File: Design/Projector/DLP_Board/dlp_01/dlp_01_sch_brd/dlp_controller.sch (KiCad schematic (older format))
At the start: 0 parts

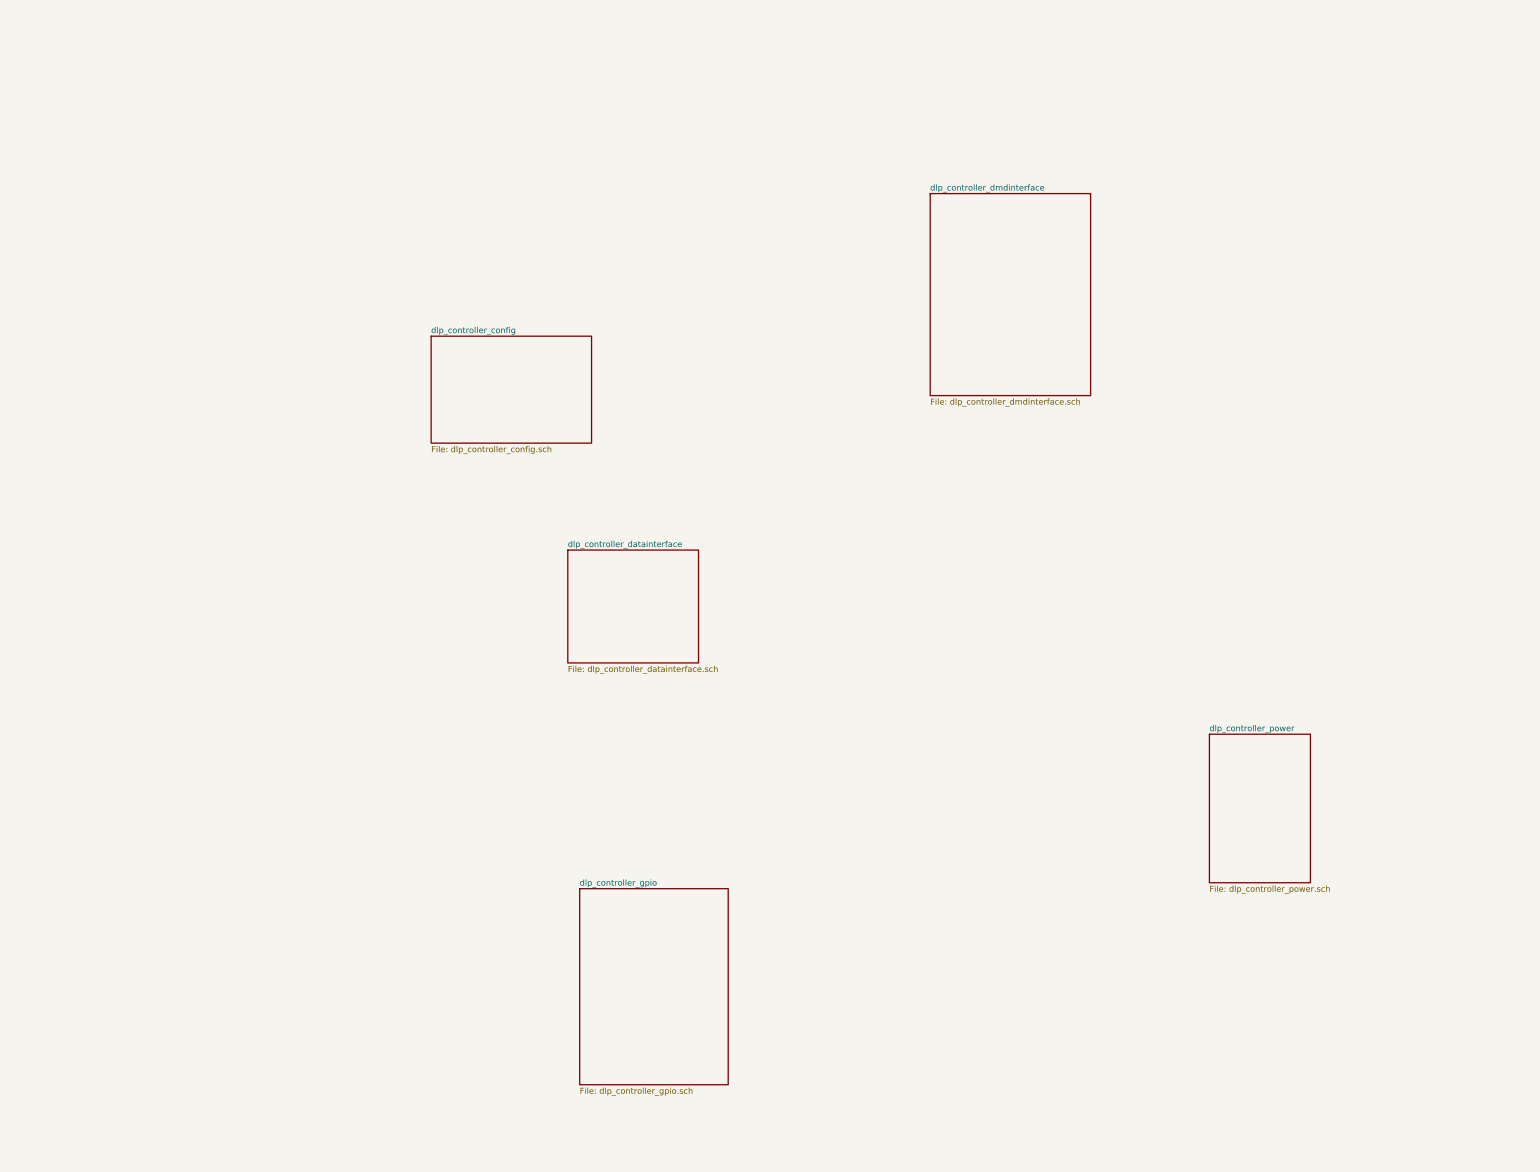
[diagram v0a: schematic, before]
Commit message: Updated schematic with changes pulling together top level design
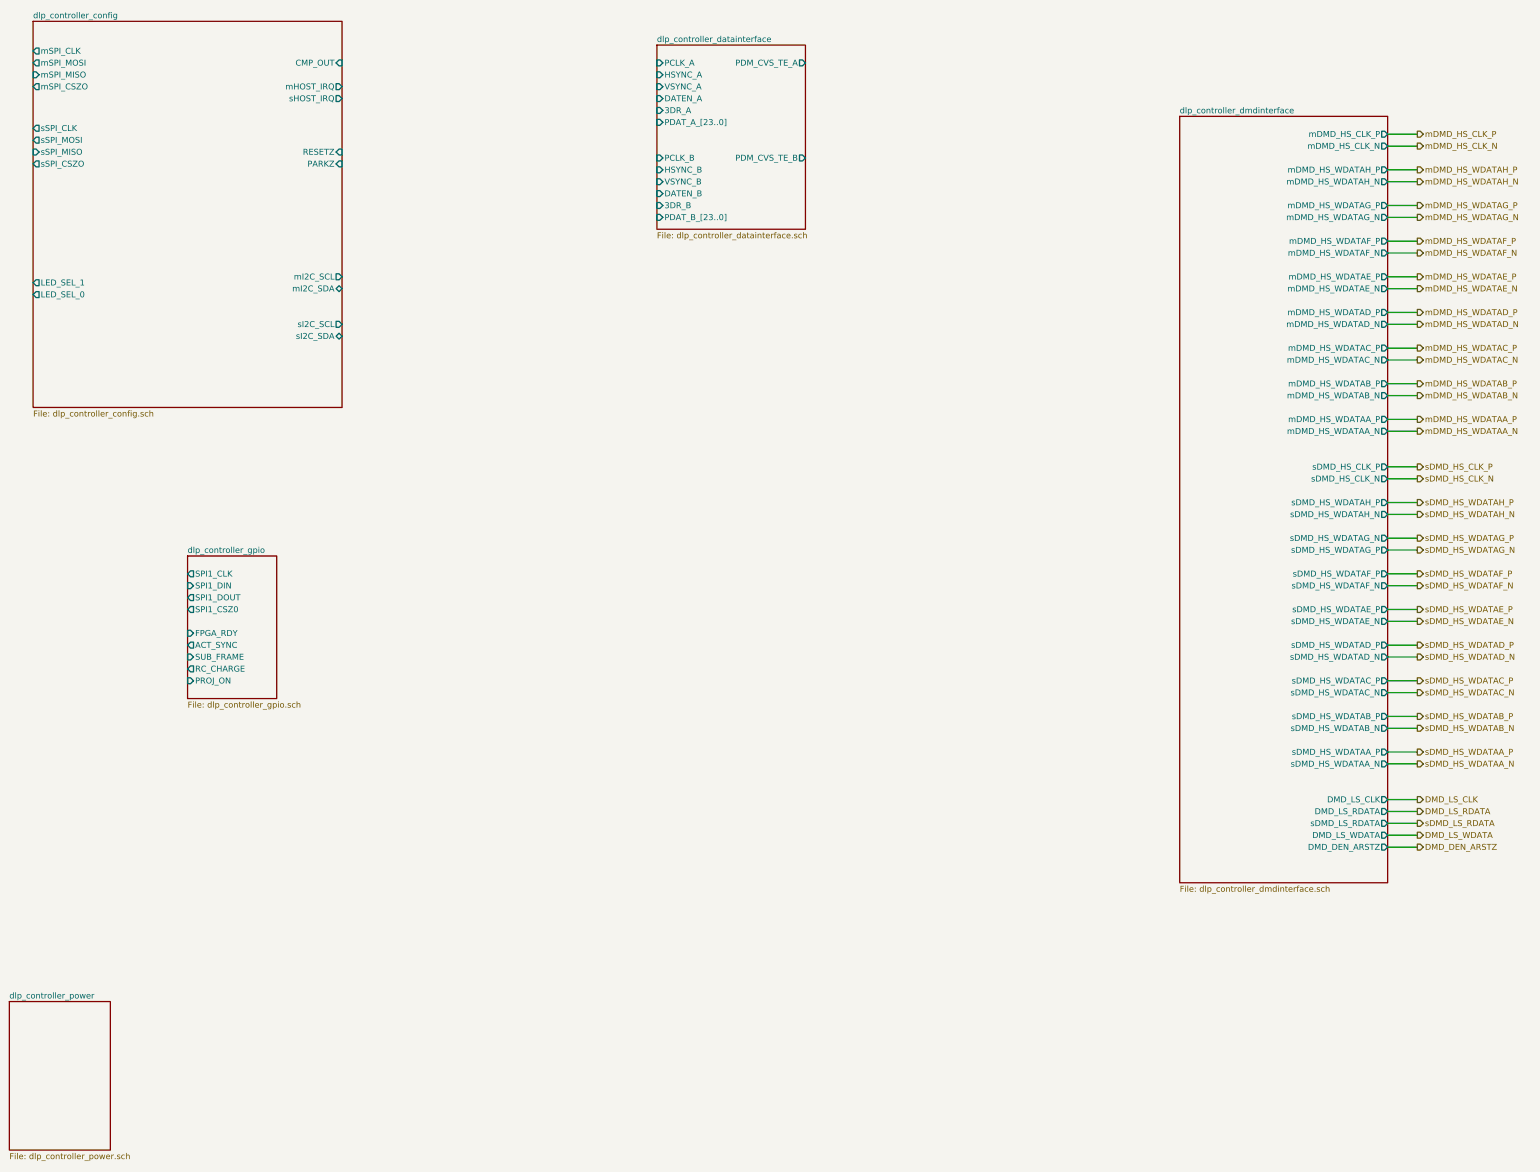
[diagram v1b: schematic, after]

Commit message: Ongoing updates the schematics
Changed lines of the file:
@@
 $EndSheet
 $Sheet
-S 1600 1050 2600 3250
+S 2350 1350 1500 2350
 U 5E32D14B
 F0 "dlp_controller_config" 50
 F1 "dlp_controller_config.sch" 50
-F2 "CMP_OUT" I R 4200 1400 50
-F3 "LED_SEL_0" O L 1600 3350 50
-F4 "LED_SEL_1" O L 1600 3250 50
-F5 "mSPI_CLK" O L 1600 1300 50
-F6 "mSPI_MOSI" O L 1600 1400 50
-F7 "mSPI_CSZO" O L 1600 1600 50
-F8 "mSPI_MISO" I L 1600 1500 50
-F9 "mI2C_SCL" O R 4200 3200 50
-F10 "mI2C_SDA" B R 4200 3300 50
-F11 "sSPI_CLK" O L 1600 1950 50
-F12 "sSPI_MOSI" O L 1600 2050 50
-F13 "sSPI_CSZO" O L 1600 2250 50
-F14 "sSPI_MISO" I L 1600 2150 50
-F15 "sI2C_SCL" O R 4200 3600 50
-F16 "sI2C_SDA" B R 4200 3700 50
-F17 "sHOST_IRQ" O R 4200 1700 50
-F18 "mHOST_IRQ" O R 4200 1600 50
-F19 "PARKZ" I R 4200 2250 50
-F20 "RESETZ" I R 4200 2150 50
+F2 "CMP_OUT" I R 3850 1700 50
+F3 "LED_SEL_0" O L 2350 3350 50
+F4 "LED_SEL_1" O L 2350 3250 50
+F5 "mSPI_CLK" O L 2350 1600 50
+F6 "mSPI_MOSI" O L 2350 1700 50
+F7 "mSPI_CSZO" O L 2350 1900 50
+F8 "mSPI_MISO" I L 2350 1800 50
+F9 "mI2C_SCL" O R 3850 2950 50
+F10 "mI2C_SDA" B R 3850 3050 50
+F11 "sSPI_CLK" O L 2350 2250 50
+F12 "sSPI_MOSI" O L 2350 2350 50
+F13 "sSPI_CSZO" O L 2350 2550 50
+F14 "sSPI_MISO" I L 2350 2450 50
+F15 "sI2C_SCL" O R 3850 3300 50
+F16 "sI2C_SDA" B R 3850 3400 50
+F17 "sHOST_IRQ" O R 3850 2000 50
+F18 "mHOST_IRQ" O R 3850 1900 50
+F19 "PARKZ" I R 3850 2550 50
+F20 "RESETZ" I R 3850 2450 50
 $EndSheet
 $Sheet
-S 6850 1250 1250 1550
+S 7600 1750 1250 1550
 U 5E8F10AD
 F0 "dlp_controller_datainterface" 50
 F1 "dlp_controller_datainterface.sch" 50
-F2 "PCLK_B" I L 6850 2200 50
-F3 "PDM_CVS_TE_B" O R 8100 2200 50
-F4 "VSYNC_B" I L 6850 2400 50
-F5 "HSYNC_B" I L 6850 2300 50
-F6 "DATEN_B" I L 6850 2500 50
-F7 "PDAT_B_[23..0]" I L 6850 2700 50
-F8 "PCLK_A" I L 6850 1400 50
-F9 "PDM_CVS_TE_A" O R 8100 1400 50
-F10 "VSYNC_A" I L 6850 1600 50
-F11 "HSYNC_A" I L 6850 1500 50
-F12 "DATEN_A" I L 6850 1700 50
-F13 "PDAT_A_[23..0]" I L 6850 1900 50
-F14 "3DR_A" I L 6850 1800 50
-F15 "3DR_B" I L 6850 2600 50
+F2 "PCLK_B" I L 7600 2700 50
+F3 "PDM_CVS_TE_B" O R 8850 2700 50
+F4 "VSYNC_B" I L 7600 2900 50
+F5 "HSYNC_B" I L 7600 2800 50
+F6 "DATEN_B" I L 7600 3000 50
+F7 "PDAT_B_[23..0]" I L 7600 3200 50
+F8 "PCLK_A" I L 7600 1900 50
+F9 "PDM_CVS_TE_A" O R 8850 1900 50
+F10 "VSYNC_A" I L 7600 2100 50
+F11 "HSYNC_A" I L 7600 2000 50
+F12 "DATEN_A" I L 7600 2200 50
+F13 "PDAT_A_[23..0]" I L 7600 2400 50
+F14 "3DR_A" I L 7600 2300 50
+F15 "3DR_B" I L 7600 3100 50
 $EndSheet
 Text HLabel 13250 2300 2    50   Output ~ 0
@@
 Wire Wire Line
 	13000 8000 13250 8000
+Text HLabel 2700 6000 0    50   Output ~ 0
+SPI1_CSZ0
+Wire Wire Line
+	2900 6000 2700 6000
+Text HLabel 2700 5900 0    50   Output ~ 0
+SPI1_DOUT
+Text HLabel 2700 5700 0    50   Output ~ 0
+SPI1_CLK
+Text HLabel 2700 5800 0    50   Input ~ 0
+SPI1_DIN
+Wire Wire Line
+	2700 5900 2900 5900
+Wire Wire Line
+	2700 5700 2900 5700
+Wire Wire Line
+	2700 5800 2900 5800
+Text HLabel 2700 6200 0    50   Input ~ 0
+FPGA_RDY
+Text HLabel 2700 6300 0    50   Output ~ 0
+ACT_SYNC
+Text HLabel 2700 6400 0    50   Input ~ 0
+SUB_FRAME
+Text HLabel 2700 6500 0    50   Output ~ 0
+RC_CHARGE
+Text HLabel 2700 6600 0    50   Input ~ 0
+PROJ_ON
+Wire Wire Line
+	2700 6200 2900 6200
+Wire Wire Line
+	2900 6300 2700 6300
+Wire Wire Line
+	2700 6400 2900 6400
+Wire Wire Line
+	2900 6500 2700 6500
+Wire Wire Line
+	2700 6600 2900 6600
+Text HLabel 7300 2700 0    50   Input ~ 0
+PCLK_B
+Text HLabel 9150 2700 2    50   Output ~ 0
+PDM_CVS_TE_B
+Text HLabel 7300 2900 0    50   Input ~ 0
+VSYNC_B
+Text HLabel 7300 2800 0    50   Input ~ 0
+HSYNC_B
+Text HLabel 7300 3000 0    50   Input ~ 0
+DATEN_B
+Text HLabel 7300 3200 0    50   Input ~ 0
+PDAT_B_[23..0]
+Text HLabel 7300 3100 0    50   Input ~ 0
+3DR_B
+Text HLabel 7300 1900 0    50   Input ~ 0
+PCLK_A
+Text HLabel 9150 1900 2    50   Output ~ 0
+PDM_CVS_TE_A
+Text HLabel 7300 2100 0    50   Input ~ 0
+VSYNC_A
+Text HLabel 7300 2000 0    50   Input ~ 0
+HSYNC_A
+Text HLabel 7300 2200 0    50   Input ~ 0
+DATEN_A
+Text HLabel 7300 2400 0    50   Input ~ 0
+PDAT_A_[23..0]
+Text HLabel 7300 2300 0    50   Input ~ 0
+3DR_A
+Wire Wire Line
+	8850 1900 9150 1900
+Wire Wire Line
+	8850 2700 9150 2700
+Wire Wire Line
+	7300 1900 7600 1900
+Wire Wire Line
+	7300 2700 7600 2700
+Wire Wire Line
+	7300 2000 7600 2000
+Wire Wire Line
+	7300 2100 7600 2100
+Wire Wire Line
+	7300 2200 7600 2200
+Wire Wire Line
+	7600 2300 7300 2300
+Wire Wire Line
+	7300 2800 7600 2800
+Wire Wire Line
+	7300 2900 7600 2900
+Wire Wire Line
+	7600 3000 7300 3000
+Wire Wire Line
+	7300 3100 7600 3100
+Wire Bus Line
+	7300 2400 7600 2400
+Wire Bus Line
+	7300 3200 7600 3200
+Text HLabel 2050 1600 0    50   Output ~ 0
+mSPI_CLK
+Text HLabel 2050 1700 0    50   Output ~ 0
+mSPI_MOSI
+Text HLabel 2050 1900 0    50   Output ~ 0
+mSPI_CSZO
+Text HLabel 2050 1800 0    50   Input ~ 0
+mSPI_MISO
+Wire Wire Line
+	2050 1600 2350 1600
+Wire Wire Line
+	2050 1700 2350 1700
+Text HLabel 4150 2950 2    50   Output ~ 0
+mI2C_SCL
+Text HLabel 4150 3050 2    50   BiDi ~ 0
+mI2C_SDA
+Text HLabel 4150 1900 2    50   Output ~ 0
+mHOST_IRQ
+Text HLabel 4150 1700 2    50   Input ~ 0
+CMP_OUT
+Text HLabel 2050 3250 0    50   Output ~ 0
+LED_SEL_0
+Text HLabel 2050 3350 0    50   Output ~ 0
+LED_SEL_1
+Text HLabel 2050 2250 0    50   Output ~ 0
+sSPI_CLK
+Text HLabel 2050 2350 0    50   Output ~ 0
+sSPI_MOSI
+Text HLabel 2050 2550 0    50   Output ~ 0
+sSPI_CSZO
+Text HLabel 2050 2450 0    50   Input ~ 0
+sSPI_MISO
+Text HLabel 4150 2000 2    50   Output ~ 0
+sHOST_IRQ
+Text HLabel 4150 3300 2    50   Output ~ 0
+sI2C_SCL
+Text HLabel 4150 3400 2    50   BiDi ~ 0
+sI2C_SDA
+Text HLabel 4150 2550 2    50   Input ~ 0
+PARKZ
+Text HLabel 4150 2450 2    50   Input ~ 0
+RESETZ
+Wire Wire Line
+	3850 1700 4150 1700
+Wire Wire Line
+	2050 1800 2350 1800
+Wire Wire Line
+	2050 1900 2350 1900
+Wire Wire Line
+	2050 2250 2350 2250
+Wire Wire Line
+	2350 2350 2050 2350
+Wire Wire Line
+	2050 2450 2350 2450
+Wire Wire Line
+	2350 2550 2050 2550
+Wire Wire Line
+	2050 3250 2350 3250
+Wire Wire Line
+	2350 3350 2050 3350
+Wire Wire Line
+	3850 1900 4150 1900
+Wire Wire Line
+	4150 2000 3850 2000
+Wire Wire Line
+	3850 2450 4150 2450
+Wire Wire Line
+	4150 2550 3850 2550
+Wire Wire Line
+	3850 2950 4150 2950
+Wire Wire Line
+	3850 3050 4150 3050
+Wire Wire Line
+	3850 3300 4150 3300
+Wire Wire Line
+	4150 3400 3850 3400
 $EndSCHEMATC

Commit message: More updates in the DLP board
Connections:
- no-connect marks 0 -> 8
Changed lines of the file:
@@
 F0 "dlp_controller_config" 50
 F1 "dlp_controller_config.sch" 50
-F2 "CMP_OUT" I R 3850 1700 50
+F2 "CMP_OUT" I R 3850 1550 50
 F3 "LED_SEL_0" O L 2350 3350 50
 F4 "LED_SEL_1" O L 2350 3250 50
@@
 F7 "mSPI_CSZO" O L 2350 1900 50
 F8 "mSPI_MISO" I L 2350 1800 50
-F9 "mI2C_SCL" O R 3850 2950 50
-F10 "mI2C_SDA" B R 3850 3050 50
-F11 "sSPI_CLK" O L 2350 2250 50
-F12 "sSPI_MOSI" O L 2350 2350 50
-F13 "sSPI_CSZO" O L 2350 2550 50
-F14 "sSPI_MISO" I L 2350 2450 50
-F15 "sI2C_SCL" O R 3850 3300 50
-F16 "sI2C_SDA" B R 3850 3400 50
-F17 "sHOST_IRQ" O R 3850 2000 50
-F18 "mHOST_IRQ" O R 3850 1900 50
-F19 "PARKZ" I R 3850 2550 50
-F20 "RESETZ" I R 3850 2450 50
+F9 "sSPI_CLK" O L 2350 2250 50
+F10 "sSPI_MOSI" O L 2350 2350 50
+F11 "sSPI_CSZO" O L 2350 2550 50
+F12 "sSPI_MISO" I L 2350 2450 50
+F13 "sHOST_IRQ" O R 3850 1850 50
+F14 "mHOST_IRQ" O R 3850 1750 50
+F15 "PARKZ" I R 3850 2200 50
+F16 "RESETZ" I R 3850 2100 50
+F17 "mI2C0_SCL" O R 3850 2450 50
+F18 "mI2C0_SDA" B R 3850 2550 50
+F19 "mI2C1_SCL" O R 3850 2750 50
+F20 "mI2C1_SDA" B R 3850 2850 50
+F21 "sI2C0_SCL" O R 3850 3100 50
+F22 "sI2C0_SDA" B R 3850 3200 50
+F23 "sI2C1_SCL" O R 3850 3400 50
+F24 "sI2C1_SDA" B R 3850 3500 50
 $EndSheet
 $Sheet
@@
 Wire Bus Line
 	7300 3200 7600 3200
-Text HLabel 2050 1600 0    50   Output ~ 0
-mSPI_CLK
-Text HLabel 2050 1700 0    50   Output ~ 0
-mSPI_MOSI
-Text HLabel 2050 1900 0    50   Output ~ 0
-mSPI_CSZO
-Text HLabel 2050 1800 0    50   Input ~ 0
-mSPI_MISO
-Wire Wire Line
-	2050 1600 2350 1600
-Wire Wire Line
-	2050 1700 2350 1700
-Text HLabel 4150 2950 2    50   Output ~ 0
-mI2C_SCL
-Text HLabel 4150 3050 2    50   BiDi ~ 0
-mI2C_SDA
-Text HLabel 4150 1900 2    50   Output ~ 0
+Text HLabel 4150 1750 2    50   Output ~ 0
 mHOST_IRQ
-Text HLabel 4150 1700 2    50   Input ~ 0
+Text HLabel 4150 1550 2    50   Input ~ 0
 CMP_OUT
 Text HLabel 2050 3250 0    50   Output ~ 0
@@
 Text HLabel 2050 3350 0    50   Output ~ 0
 LED_SEL_1
-Text HLabel 2050 2250 0    50   Output ~ 0
-sSPI_CLK
-Text HLabel 2050 2350 0    50   Output ~ 0
-sSPI_MOSI
-Text HLabel 2050 2550 0    50   Output ~ 0
-sSPI_CSZO
-Text HLabel 2050 2450 0    50   Input ~ 0
-sSPI_MISO
-Text HLabel 4150 2000 2    50   Output ~ 0
+Text HLabel 4150 1850 2    50   Output ~ 0
 sHOST_IRQ
-Text HLabel 4150 3300 2    50   Output ~ 0
-sI2C_SCL
-Text HLabel 4150 3400 2    50   BiDi ~ 0
-sI2C_SDA
+Text HLabel 4150 2200 2    50   Input ~ 0
+PARKZ
+Text HLabel 4150 2100 2    50   Input ~ 0
+RESETZ
+Wire Wire Line
+	3850 1550 4150 1550
+Wire Wire Line
+	2050 3250 2350 3250
+Wire Wire Line
+	2350 3350 2050 3350
+Wire Wire Line
+	3850 1750 4150 1750
+Wire Wire Line
+	4150 1850 3850 1850
+Wire Wire Line
+	3850 2100 4150 2100
+Wire Wire Line
+	4150 2200 3850 2200
+Wire Wire Line
+	3850 2450 4150 2450
+Wire Wire Line
+	3850 2550 4150 2550
+Wire Wire Line
+	3850 2750 3950 2750
+Wire Wire Line
+	4050 2850 3850 2850
+Wire Wire Line
+	3850 3100 3950 3100
+Wire Wire Line
+	3950 3100 3950 2750
+Wire Wire Line
+	3850 3200 4050 3200
+Wire Wire Line
+	4050 3200 4050 2850
+Text HLabel 4150 2450 2    50   Input ~ 0
+HOST_SCL
 Text HLabel 4150 2550 2    50   Input ~ 0
-PARKZ
-Text HLabel 4150 2450 2    50   Input ~ 0
-RESETZ
-Wire Wire Line
-	3850 1700 4150 1700
-Wire Wire Line
-	2050 1800 2350 1800
-Wire Wire Line
-	2050 1900 2350 1900
-Wire Wire Line
-	2050 2250 2350 2250
-Wire Wire Line
-	2350 2350 2050 2350
-Wire Wire Line
-	2050 2450 2350 2450
-Wire Wire Line
-	2350 2550 2050 2550
-Wire Wire Line
-	2050 3250 2350 3250
-Wire Wire Line
-	2350 3350 2050 3350
-Wire Wire Line
-	3850 1900 4150 1900
-Wire Wire Line
-	4150 2000 3850 2000
-Wire Wire Line
-	3850 2450 4150 2450
-Wire Wire Line
-	4150 2550 3850 2550
-Wire Wire Line
-	3850 2950 4150 2950
-Wire Wire Line
-	3850 3050 4150 3050
-Wire Wire Line
-	3850 3300 4150 3300
-Wire Wire Line
-	4150 3400 3850 3400
+HOST_SDA
+Text HLabel 4150 2750 2    50   Input ~ 0
+CONTR0_SCL
+Text HLabel 4150 2850 2    50   BiDi ~ 0
+CONTR0_SDA
+Text HLabel 4150 3500 2    50   BiDi ~ 0
+CONTR1_SDA
+Text HLabel 4150 3400 2    50   Input ~ 0
+CONTR1_SCL
+Wire Wire Line
+	3950 2750 4150 2750
+Connection ~ 3950 2750
+Wire Wire Line
+	4050 2850 4150 2850
+Connection ~ 4050 2850
+Wire Wire Line
+	3850 3400 4150 3400
+Wire Wire Line
+	3850 3500 4150 3500
+NoConn ~ 2350 1600
+NoConn ~ 2350 1700
+NoConn ~ 2350 1800
+NoConn ~ 2350 1900
+NoConn ~ 2350 2250
+NoConn ~ 2350 2350
+NoConn ~ 2350 2450
+NoConn ~ 2350 2550
 $EndSCHEMATC
